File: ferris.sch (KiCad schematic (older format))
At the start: 95 parts, among them J1 USB C, K0_0 KEYSW, K0_1 KEYSW, K0_2 KEYSW, K0_3 KEYSW, K0_4 KEYSW, K0_5 KEYSW, K0_6 KEYSW, K0_7 KEYSW, K0_8 KEYSW, K0_9 KEYSW, K1_0 KEYSW, K1_1 KEYSW, K1_2 KEYSW, K1_3 KEYSW, K1_4 KEYSW, K1_5 KEYSW, K1_6 KEYSW, K1_7 KEYSW, K1_8 KEYSW, K1_9 KEYSW, K2_0 KEYSW, K2_1 KEYSW, K2_2 KEYSW, K2_3 KEYSW, K2_4 KEYSW, K2_5 KEYSW, K2_6 KEYSW, K2_7 KEYSW, K2_8 KEYSW, K2_9 KEYSW, K3_3 KEYSW, K3_4 KEYSW, K3_5 KEYSW, K3_6 KEYSW, SW1 SW_PUSH, U1 ATmega32U4-AU, U2 MCP23017_SO, Y1 Crystal

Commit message: Added LED on LHS
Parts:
- added D1: WS2812B, LED_SMD:LED_WS2812B_PLCC4_5.0x5.0mm_P3.2mm, symbol LED:WS2812B
- added U3: TCA9535RTWR, Package_DFN_QFN:WQFN-24-1EP_4x4mm_P0.5mm_EP2.45x2.45mm, symbol Interface_Expansion:TCA9535RTWR
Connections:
- wire segments 125 -> 130
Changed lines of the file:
@@
 NoConn ~ 4150 6900
 NoConn ~ 4150 6800
-NoConn ~ 4150 6700
 Connection ~ 10000 6350
 Wire Wire Line
@@
 L power:GND #PWR0106
 U 1 1 5F0D6F7A
-P 4700 5700
-F 0 "#PWR0106" H 4700 5750 20  0001 C CNN
-F 1 "GND" H 4750 5650 30  0000 L CNN
-F 2 "" H 4700 5700 60  0000 C CNN
-F 3 "" H 4700 5700 60  0000 C CNN
-	1    4700 5700
+P 4700 6050
+F 0 "#PWR0106" H 4700 6100 20  0001 C CNN
+F 1 "GND" H 4750 6000 30  0000 L CNN
+F 2 "" H 4700 6050 60  0000 C CNN
+F 3 "" H 4700 6050 60  0000 C CNN
+	1    4700 6050
 	1    0    0    -1
 $EndComp
@@
 	0    -1   -1   0
 $EndComp
+Wire Wire Line
+	4700 5700 4700 6050
+$Comp
+L Interface_Expansion:TCA9535RTWR U3
+U 1 1 5F24632D
+P 6800 5200
+F 0 "U3" H 6800 6481 50  0000 C CNN
+F 1 "TCA9535RTWR" H 6800 6390 50  0000 C CNN
+F 2 "Package_DFN_QFN:WQFN-24-1EP_4x4mm_P0.5mm_EP2.45x2.45mm" H 8000 4200 50  0001 C CNN
+F 3 "http://www.ti.com/lit/ds/symlink/tca9535.pdf" H 6300 6100 50  0001 C CNN
+	1    6800 5200
+	1    0    0    -1
+$EndComp
+$Comp
+L LED:WS2812B D1
+U 1 1 5F237653
+P 5250 3700
+F 0 "D1" H 5594 3746 50  0000 L CNN
+F 1 "WS2812B" H 5594 3655 50  0000 L CNN
+F 2 "LED_SMD:LED_WS2812B_PLCC4_5.0x5.0mm_P3.2mm" H 5300 3400 50  0001 L TNN
+F 3 "https://cdn-shop.adafruit.com/datasheets/WS2812B.pdf" H 5350 3325 50  0001 L TNN
+	1    5250 3700
+	1    0    0    -1
+$EndComp
+Wire Wire Line
+	5250 3400 3550 3400
+Wire Wire Line
+	3550 3400 3550 3900
+$Comp
+L power:GND #PWR0118
+U 1 1 5F2446EA
+P 5250 4000
+F 0 "#PWR0118" H 5250 4050 20  0001 C CNN
+F 1 "GND" H 5300 3950 30  0000 L CNN
+F 2 "" H 5250 4000 60  0000 C CNN
+F 3 "" H 5250 4000 60  0000 C CNN
+	1    5250 4000
+	1    0    0    -1
+$EndComp
+Wire Wire Line
+	4150 6700 4950 6700
+Wire Wire Line
+	4950 6700 4950 3700
+NoConn ~ 5550 3700
 $EndSCHEMATC

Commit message: Moved I2C resistors to RHS, moved LED
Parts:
- removed U3: TCA9535RTWR, Package_DFN_QFN:WQFN-24-1EP_4x4mm_P0.5mm_EP2.45x2.45mm, symbol Interface_Expansion:TCA9535RTWR
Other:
- moved on the sheet: R7, R8
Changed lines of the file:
@@
 L Device:R R7
 U 1 1 60281202
-P 4550 5250
-F 0 "R7" V 4650 5200 50  0000 C CNN
-F 1 "4.7k" V 4550 5250 50  0000 C CNN
-F 2 "Resistor_SMD:R_0805_2012Metric_Pad1.15x1.40mm_HandSolder" V 4480 5250 50  0001 C CNN
-F 3 "~" H 4550 5250 50  0001 C CNN
-F 4 "C17673" V 4550 5250 50  0001 C CNN "LCSC Part #"
-	1    4550 5250
+P 8750 4300
+F 0 "R7" V 8850 4250 50  0000 C CNN
+F 1 "4.7k" V 8750 4300 50  0000 C CNN
+F 2 "Resistor_SMD:R_0805_2012Metric_Pad1.15x1.40mm_HandSolder" V 8680 4300 50  0001 C CNN
+F 3 "~" H 8750 4300 50  0001 C CNN
+F 4 "C17673" V 8750 4300 50  0001 C CNN "LCSC Part #"
+	1    8750 4300
 	-1   0    0    1
 $EndComp
@@
 L Device:R R8
 U 1 1 602A653D
-P 4550 5650
-F 0 "R8" V 4650 5700 50  0000 C CNN
-F 1 "4.7k" V 4550 5650 50  0000 C CNN
-F 2 "Resistor_SMD:R_0805_2012Metric_Pad1.15x1.40mm_HandSolder" V 4480 5650 50  0001 C CNN
-F 3 "~" H 4550 5650 50  0001 C CNN
-	1    4550 5650
+P 9000 4400
+F 0 "R8" V 9100 4450 50  0000 C CNN
+F 1 "4.7k" V 9000 4400 50  0000 C CNN
+F 2 "Resistor_SMD:R_0805_2012Metric_Pad1.15x1.40mm_HandSolder" V 8930 4400 50  0001 C CNN
+F 3 "~" H 9000 4400 50  0001 C CNN
+	1    9000 4400
 	-1   0    0    1
 $EndComp
 Wire Wire Line
-	8600 4150 10000 4150
+	8600 4150 8750 4150
 Wire Wire Line
 	8450 6350 9300 6350
@@
 	8350 4350 8600 4350
 Wire Wire Line
-	8350 4450 9300 4450
+	8350 4450 8750 4450
 $Comp
 L Connector:AudioJack4 Jack1
@@
 $EndComp
 Wire Wire Line
-	8350 4550 9300 4550
+	8350 4550 9000 4550
 $Comp
 L power:VDD #PWR0126
@@
 Connection ~ 2350 6000
 Wire Wire Line
-	4150 5400 4550 5400
-Wire Wire Line
-	4150 5500 4550 5500
-Connection ~ 4550 5400
-Wire Wire Line
-	4550 5400 4700 5400
-Connection ~ 4550 5500
-Wire Wire Line
-	4550 5500 4700 5500
-Wire Wire Line
-	4550 5800 4650 5800
-Wire Wire Line
-	4650 5800 4650 5600
-Wire Wire Line
 	4700 5600 4650 5600
-Connection ~ 4650 5600
-Wire Wire Line
-	4550 5100 4650 5100
 NoConn ~ 4150 4200
 NoConn ~ 4150 4900
@@
 	1    0    0    -1
 $EndComp
-Connection ~ 4650 5100
 $Comp
 L power:PWR_FLAG #FLG0101
@@
 	4700 5700 4700 6050
 $Comp
-L Interface_Expansion:TCA9535RTWR U3
-U 1 1 5F24632D
-P 6800 5200
-F 0 "U3" H 6800 6481 50  0000 C CNN
-F 1 "TCA9535RTWR" H 6800 6390 50  0000 C CNN
-F 2 "Package_DFN_QFN:WQFN-24-1EP_4x4mm_P0.5mm_EP2.45x2.45mm" H 8000 4200 50  0001 C CNN
-F 3 "http://www.ti.com/lit/ds/symlink/tca9535.pdf" H 6300 6100 50  0001 C CNN
-	1    6800 5200
-	1    0    0    -1
-$EndComp
-$Comp
 L LED:WS2812B D1
 U 1 1 5F237653
@@
 	4950 6700 4950 3700
 NoConn ~ 5550 3700
+Connection ~ 8750 4450
+Wire Wire Line
+	8750 4450 9300 4450
+Connection ~ 8750 4150
+Wire Wire Line
+	8750 4150 9000 4150
+Connection ~ 9000 4550
+Wire Wire Line
+	9000 4550 9300 4550
+Wire Wire Line
+	9000 4250 9000 4150
+Wire Wire Line
+	4150 5400 4700 5400
+Wire Wire Line
+	4150 5500 4700 5500
+Connection ~ 9000 4150
+Wire Wire Line
+	9000 4150 10000 4150
 $EndSCHEMATC

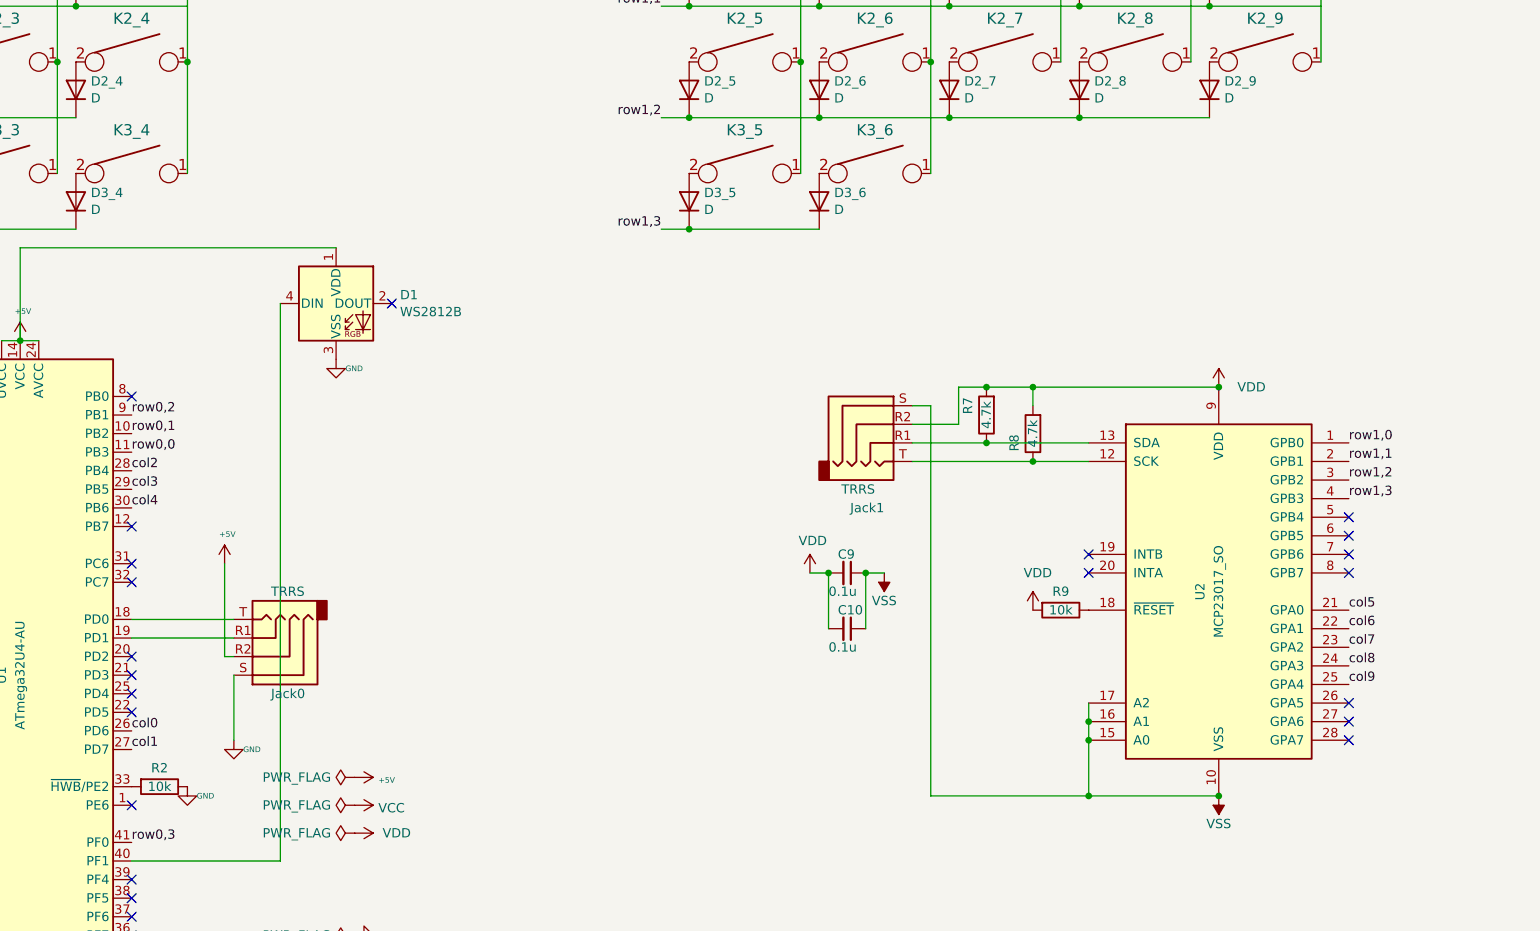
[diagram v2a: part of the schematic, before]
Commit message: Replaced MCP23017 with PCA9539PW
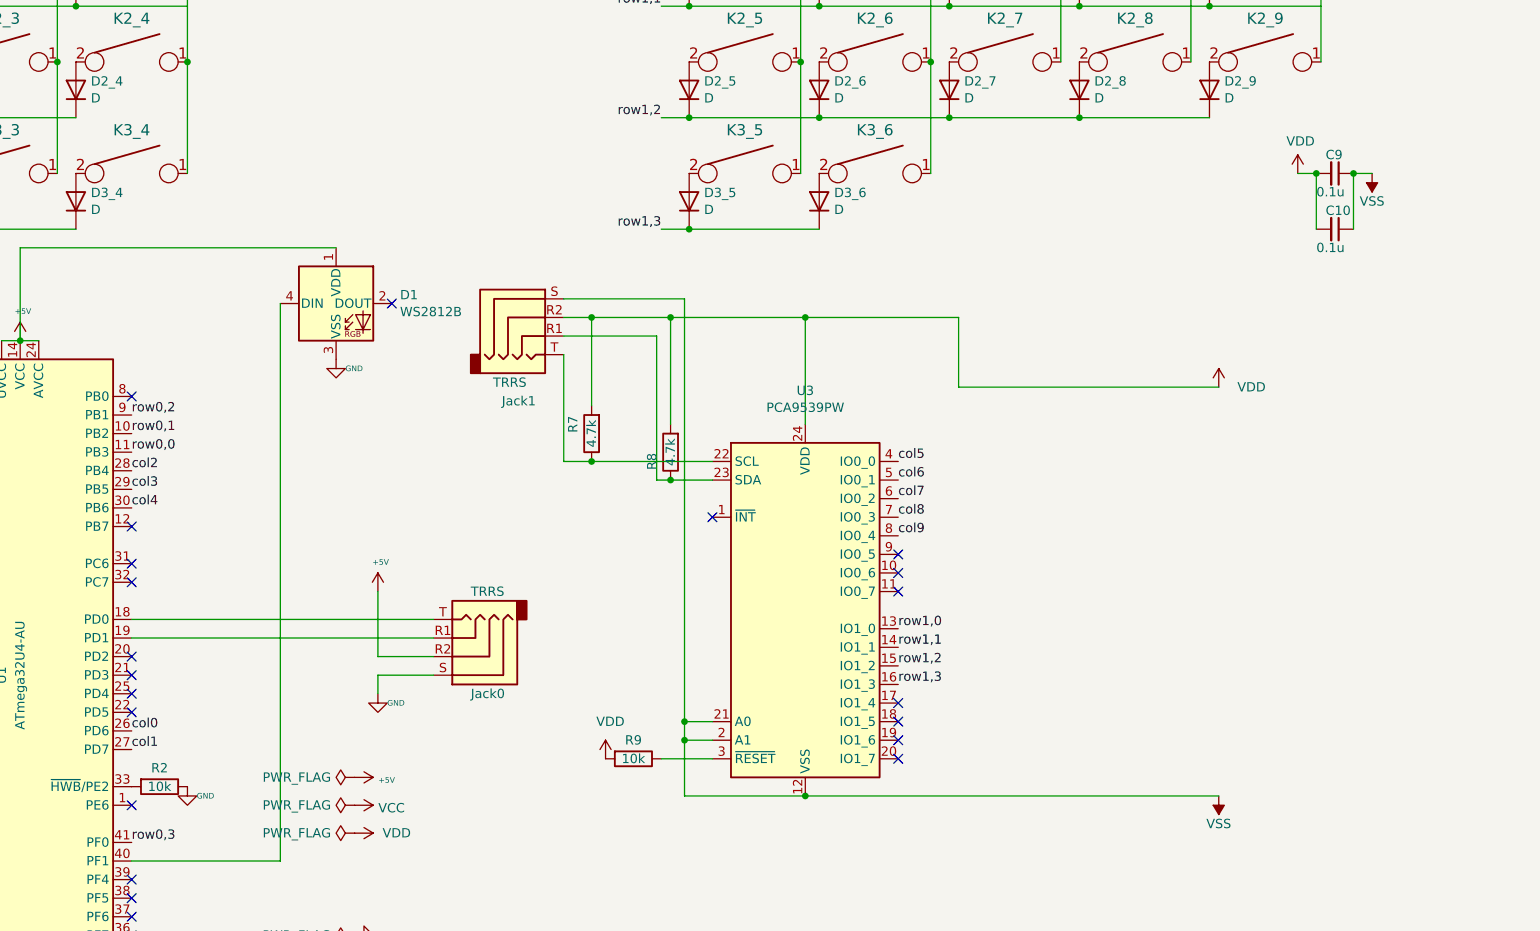
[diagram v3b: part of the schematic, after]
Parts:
- removed U2: MCP23017_SO, Package_SO:SOIC-28W_7.5x17.9mm_P1.27mm, symbol Interface_Expansion:MCP23017_SO
- added U3: PCA9539PW, Package_SO:TSSOP-24_4.4x7.8mm_P0.65mm, symbol Interface_Expansion:PCA9539PW
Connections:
- wire segments 130 -> 139
- no-connect marks 27 -> 26
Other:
- moved on the sheet: C10, C9, Jack0, Jack1, R7, R8, R9

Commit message: Repositioned the components near the inner edges
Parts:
- U3: symbol Interface_Expansion:PCA9539PW -> ferris-rescue:PCA9539PW-Interface_Expansion
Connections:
- wire segments 139 -> 138
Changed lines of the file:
@@
 L power:VDD #PWR0126
 U 1 1 5EE420B1
-P 10000 4150
-F 0 "#PWR0126" H 10000 4000 50  0001 C CNN
-F 1 "VDD" H 10100 4150 50  0000 L CNN
-F 2 "" H 10000 4150 50  0001 C CNN
-F 3 "" H 10000 4150 50  0001 C CNN
-	1    10000 4150
+P 7750 3700
+F 0 "#PWR0126" H 7750 3550 50  0001 C CNN
+F 1 "VDD" H 7850 3700 50  0000 L CNN
+F 2 "" H 7750 3700 50  0001 C CNN
+F 3 "" H 7750 3700 50  0001 C CNN
+	1    7750 3700
 	1    0    0    -1
 $EndComp
@@
 L power:VSS #PWR0121
 U 1 1 5F05F2A6
-P 10000 6350
-F 0 "#PWR0121" H 10000 6200 50  0001 C CNN
-F 1 "VSS" H 10000 6500 50  0000 C CNN
-F 2 "" H 10000 6350 50  0001 C CNN
-F 3 "" H 10000 6350 50  0001 C CNN
-	1    10000 6350
+P 8250 6350
+F 0 "#PWR0121" H 8250 6200 50  0001 C CNN
+F 1 "VSS" H 8250 6500 50  0000 C CNN
+F 2 "" H 8250 6350 50  0001 C CNN
+F 3 "" H 8250 6350 50  0001 C CNN
+	1    8250 6350
 	-1   0    0    1
 $EndComp
@@
 	5475 5700 5775 5700
 $Comp
-L Interface_Expansion:PCA9539PW U3
+L ferris-rescue:PCA9539PW-Interface_Expansion U3
 U 1 1 5F351AF3
 P 7775 5350
@@
 Connection ~ 7050 3775
 Wire Wire Line
-	7050 3775 7775 3775
+	7050 3775 7750 3775
 NoConn ~ 7275 4850
 NoConn ~ 8275 5050
@@
 NoConn ~ 8275 6150
 Wire Wire Line
-	8600 4150 10000 4150
-Wire Wire Line
-	7775 6350 10000 6350
-Wire Wire Line
-	7775 3775 8600 3775
-Wire Wire Line
-	8600 3775 8600 4150
-Connection ~ 7775 3775
+	7775 6350 8250 6350
+Wire Wire Line
+	7750 3700 7750 3775
+Connection ~ 7750 3775
+Wire Wire Line
+	7750 3775 7775 3775
 $EndSCHEMATC
